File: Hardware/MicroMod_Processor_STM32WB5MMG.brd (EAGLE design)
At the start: 22 x 22 mm, 28 parts, among them J1 MICROMOD-2222, Q1 20V/4.2A/52mΩ/1.4W, U1 STM32WB5MMG, U2 W25QXX128MBIT-6X5

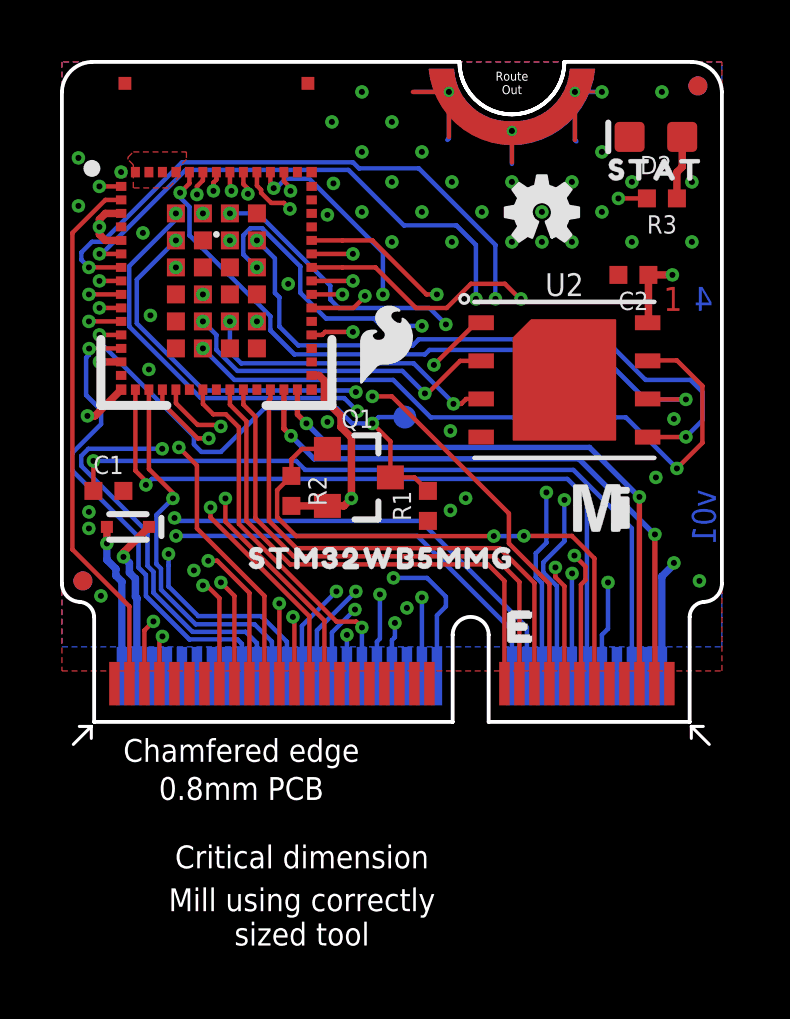
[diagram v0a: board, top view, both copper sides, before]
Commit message: Update for v10
Changelog from v01:
* Connect unused GPIO to ground
** AN4899
** Reduces power consumption and noise
* Add ESD to USB data lines
** This module is sensitive to it
** Moved Flash chip up to make room for ESD diode package
* Set text objects to spin
** When panelizing, the upside down ones didn’t spin on protos so I fixed that
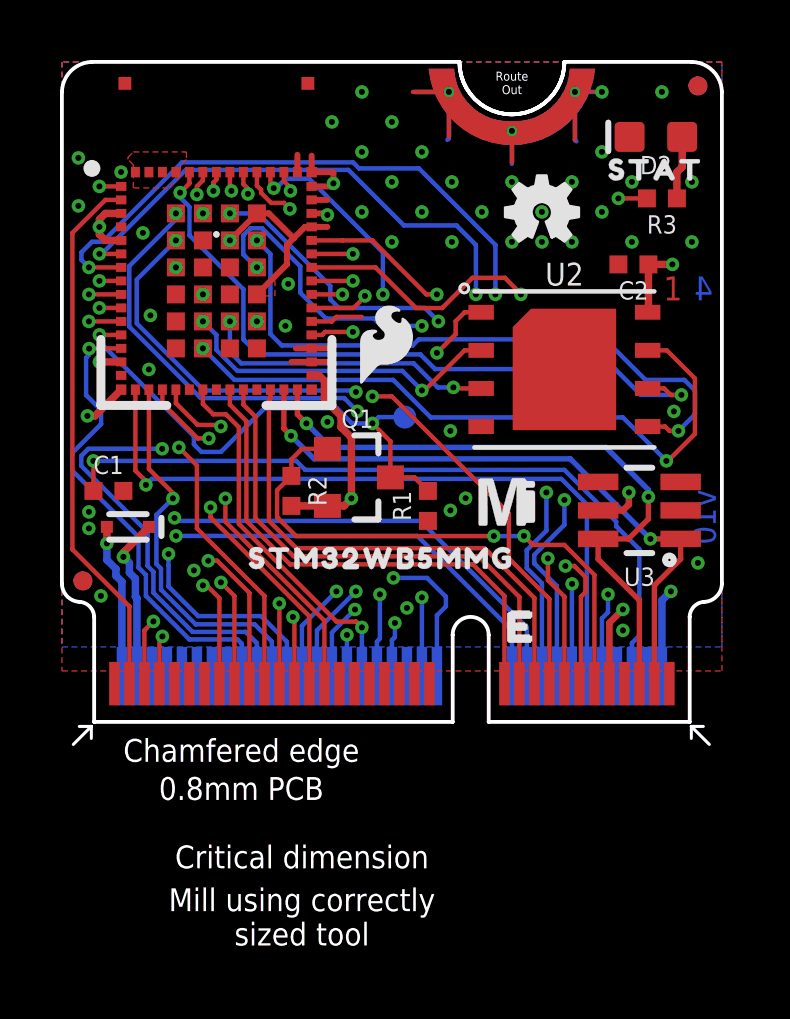
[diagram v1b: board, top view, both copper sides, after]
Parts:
- added U3: ESD Diode, SparkFun-DiscreteSemi:SOT-23-6
- moved U$1 3.16 mm to (14.8, 7.35)
- moved C2 0.35 mm to (19.1, 15.2)
- moved U2 0.35 mm to (16.8, 11.8)
- moved LOGO3 0.10 mm to (15.7, 11.9)
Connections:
- new net N$2: J1.9, U3.5
- net GND: now also U1.22, U1.24, U1.27, U1.33, U1.34, U1.36, U1.43, U1.44, U1.45, U1.46, U1.47, U1.48, U1.64, U1.65, U1.66, U1.68, U1.69, U1.71, U1.74, U1.77, U1.78, U1.82, U1.83, U3.2
- net USB_N: now also U3.6
- net USB_P: now also U3.1
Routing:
- net GND: track 11.8 -> 26.4 mm, vias 44 -> 45
- net N$2: track 0.00 -> 8.15 mm, vias 0 -> 2
- net USB_N: track 19.6 -> 21.9 mm
- net USB_P: track 20.1 -> 21.2 mm
- net 3.3V: track 22.1 -> 21.1 mm
- net QSPI_IO3: track 22.7 -> 22.1 mm
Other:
- board text added: "Material: TG155"
- board text added: "Solder Mask: Red"
- board text added: "Stackup: JLC7628"
- board text added: "Thickness: 0.8mm"
- board text added: "v10"
- board text removed: "Board Thickness is 0.8mm"
- board text removed: "v01"

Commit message: v10 Update
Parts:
- removed U3: ESD Diode, SparkFun-DiscreteSemi:SOT-23-6
- added D3: PRTR5V0U2F, SparkFun-IC-Power:SOT886
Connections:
- removed net N$2: J1.9, U3.5
- new net N$4: D3.5, J1.9
- new net USBIN_N: D3.4, J1.5
- new net USBIN_P: D3.6, J1.3
- net GND: now also D3.2; no longer U3.2
- net USB_N: now also D3.3; no longer J1.5, U3.6
- net USB_P: now also D3.1; no longer J1.3, U3.1
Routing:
- net N$2: track 8.15 -> 0.00 mm, vias 2 -> 0
- net USB_N: track 21.9 -> 14.2 mm
- net USB_P: track 21.2 -> 15.3 mm
- net N$4: track 0.00 -> 5.55 mm, vias 0 -> 2
- net USBIN_N: track 0.00 -> 5.21 mm
- net USBIN_P: track 0.00 -> 5.21 mm
- net GND: track 26.4 -> 28.6 mm, vias 45 -> 49
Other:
- board text added: "Units in mm."
